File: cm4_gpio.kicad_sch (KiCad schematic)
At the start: 37 parts, among them CN3 Harwin M20-9990246, U3 SN74LVC1G125DBV

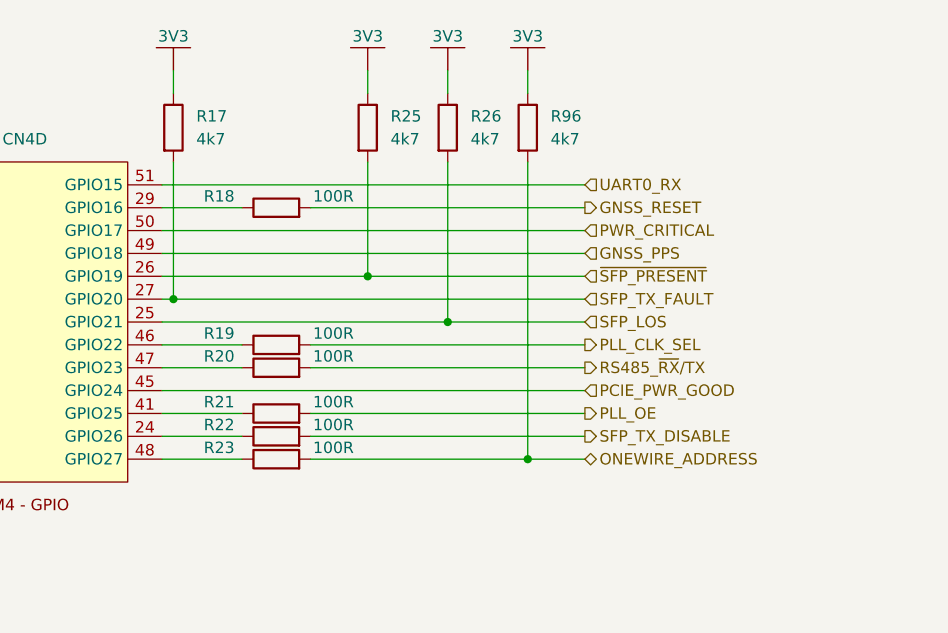
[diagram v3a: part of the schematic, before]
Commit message: Think complete - apart from 12V connection
Removed accidential step file
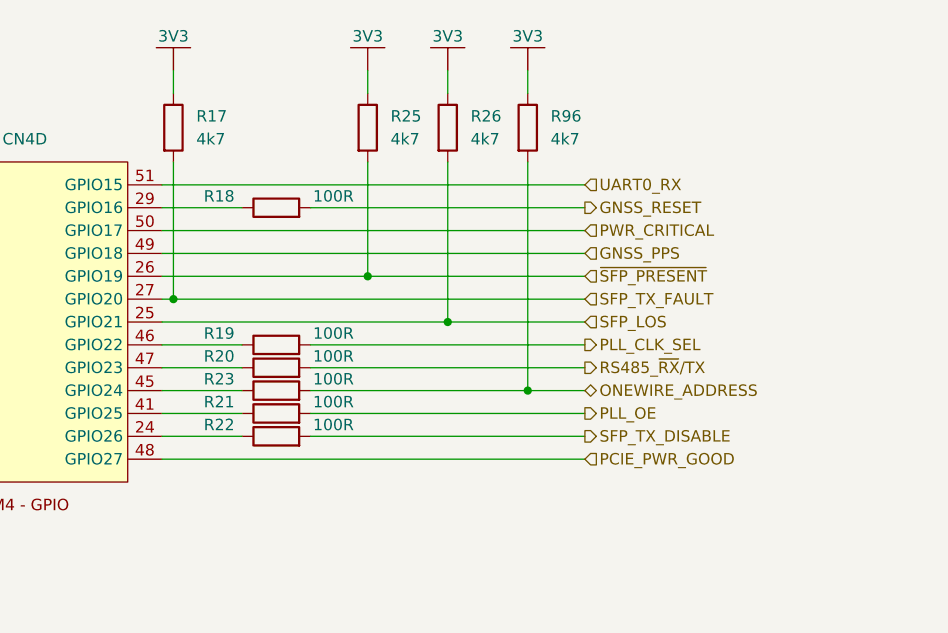
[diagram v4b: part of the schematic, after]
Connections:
- net PCIE_PWR_GOOD: now also CN4.48 (GPIO27); no longer CN4.45 (GPIO24)
- net at R23.1: now also CN4.45 (GPIO24); no longer CN4.48 (GPIO27)
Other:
- moved on the sheet: R23
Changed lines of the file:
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@@
   (junction (at 171.45 212.09) (diameter 0) (color 0 0 0 0)
   )
-  (junction (at 259.08 86.36) (diameter 0) (color 0 0 0 0)
-  )
   (junction (at 262.89 212.09) (diameter 0) (color 0 0 0 0)
   )
@@
   )
   (junction (at 162.56 200.66) (diameter 0) (color 0 0 0 0)
+  )
+  (junction (at 259.08 78.74) (diameter 0) (color 0 0 0 0)
   )
   (junction (at 222.25 240.03) (diameter 0) (color 0 0 0 0)
@@
     (stroke (width 0) (type default))
   )
+  (wire (pts (xy 218.44 86.36) (xy 265.43 86.36))
+    (stroke (width 0) (type default))
+  )
   (wire (pts (xy 250.19 71.12) (xy 265.43 71.12))
     (stroke (width 0) (type default))
@@
     (stroke (width 0) (type default))
   )
-  (wire (pts (xy 259.08 53.34) (xy 259.08 86.36))
-    (stroke (width 0) (type default))
-  )
   (wire (pts (xy 171.45 207.01) (xy 173.99 207.01))
     (stroke (width 0) (type default))
@@
     (stroke (width 0) (type default))
   )
-  (wire (pts (xy 259.08 86.36) (xy 265.43 86.36))
-    (stroke (width 0) (type default))
-  )
   (wire (pts (xy 240.03 133.35) (xy 240.03 135.89))
     (stroke (width 0) (type default))
   )
+  (wire (pts (xy 259.08 78.74) (xy 265.43 78.74))
+    (stroke (width 0) (type default))
+  )
   (wire (pts (xy 234.95 58.42) (xy 265.43 58.42))
     (stroke (width 0) (type default))
@@
     (stroke (width 0) (type default))
   )
-  (wire (pts (xy 218.44 78.74) (xy 265.43 78.74))
+  (wire (pts (xy 218.44 78.74) (xy 227.33 78.74))
     (stroke (width 0) (type default))
   )
@@
     (stroke (width 0) (type default))
   )
+  (wire (pts (xy 259.08 53.34) (xy 259.08 78.74))
+    (stroke (width 0) (type default))
+  )
   (wire (pts (xy 242.57 204.47) (xy 242.57 207.01))
     (stroke (width 0) (type default))
@@
     (stroke (width 0) (type default))
   )
-  (wire (pts (xy 218.44 86.36) (xy 227.33 86.36))
-    (stroke (width 0) (type default))
-  )
   (wire (pts (xy 250.19 53.34) (xy 250.19 71.12))
     (stroke (width 0) (type default))
@@
     (stroke (width 0) (type default))
   )
-  (wire (pts (xy 234.95 86.36) (xy 259.08 86.36))
-    (stroke (width 0) (type default))
-  )
   (wire (pts (xy 209.55 240.03) (xy 212.09 240.03))
     (stroke (width 0) (type default))
@@
   )
   (wire (pts (xy 242.57 212.09) (xy 251.46 212.09))
+    (stroke (width 0) (type default))
+  )
+  (wire (pts (xy 234.95 78.74) (xy 259.08 78.74))
     (stroke (width 0) (type default))
   )
@@
     (effects (font (size 1.27 1.27)) (justify left bottom))
   )
-  (hierarchical_label "PCIE_PWR_GOOD" (shape input) (at 265.43 78.74 0) (fields_autoplaced)
+  (hierarchical_label "PCIE_PWR_GOOD" (shape input) (at 265.43 86.36 0) (fields_autoplaced)
     (effects (font (size 1.27 1.27)) (justify left))
   )
@@
     (effects (font (size 1.27 1.27)) (justify left))
   )
-  (hierarchical_label "ONEWIRE_ADDRESS" (shape bidirectional) (at 265.43 86.36 0) (fields_autoplaced)
+  (hierarchical_label "ONEWIRE_ADDRESS" (shape bidirectional) (at 265.43 78.74 0) (fields_autoplaced)
     (effects (font (size 1.27 1.27)) (justify left))
   )
@@
     )
   )
-  (symbol (lib_id "AAA_Preferred_WUT:KOA Speer RK73H1ETTP1000F") (at 231.14 86.36 90) (unit 1)
+  (symbol (lib_id "AAA_Preferred_WUT:KOA Speer RK73H1ETTP1000F") (at 231.14 78.74 90) (unit 1)
     (in_bom yes) (on_board yes) (dnp no)
-    (property "Reference" "R23" (at 224.79 85.09 90)
-      (effects (font (size 1.27 1.27)))
-    )
-    (property "Value" "100R" (at 237.49 85.09 90)
-      (effects (font (size 1.27 1.27)))
-    )
-    (property "Footprint" "Resistor_SMD:R_0402_1005Metric" (at 231.14 88.138 90)
-      (effects (font (size 1.27 1.27)) hide)
-    )
-    (property "Datasheet" "https://www.koaspeer.com/pdfs/RK73H.pdf" (at 231.14 86.36 0)
-      (effects (font (size 1.27 1.27)) hide)
-    )
-    (property "MPN" "RK73H1ETTP1000F" (at 231.14 86.36 0)
-      (effects (font (size 1.27 1.27)) hide)
-    )
-    (property "Manufacturer" "KOA Speer" (at 231.14 86.36 0)
-      (effects (font (size 1.27 1.27)) hide)
-    )
-    (property "Tolerance" "1%" (at 231.14 86.36 0)
-      (effects (font (size 1.27 1.27)) hide)
-    )
-    (property "Height" "0.4mm" (at 231.14 86.36 0)
-      (effects (font (size 1.27 1.27)) hide)
-    )
+    (property "Reference" "R23" (at 224.79 77.47 90)
+      (effects (font (size 1.27 1.27)))
+    )
+    (property "Value" "100R" (at 237.49 77.47 90)
+      (effects (font (size 1.27 1.27)))
+    )
+    (property "Footprint" "Resistor_SMD:R_0402_1005Metric" (at 231.14 80.518 90)
+      (effects (font (size 1.27 1.27)) hide)
+    )
+    (property "Datasheet" "https://www.koaspeer.com/pdfs/RK73H.pdf" (at 231.14 78.74 0)
+      (effects (font (size 1.27 1.27)) hide)
+    )
+    (property "MPN" "RK73H1ETTP1000F" (at 231.14 78.74 0)
+      (effects (font (size 1.27 1.27)) hide)
+    )
+    (property "Manufacturer" "KOA Speer" (at 231.14 78.74 0)
+      (effects (font (size 1.27 1.27)) hide)
+    )
+    (property "Tolerance" "1%" (at 231.14 78.74 0)
+      (effects (font (size 1.27 1.27)) hide)
+    )
+    (property "Height" "0.4mm" (at 231.14 78.74 0)
+      (effects (font (size 1.27 1.27)) hide)
+    )
